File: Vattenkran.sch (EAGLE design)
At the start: 25 parts, among them J1 Power Module, J2 AVR_SPI_PRG_6OFFSET_PADS, J3 DHT11, J4 Wakeup Button, J5 RESONATOR, J6 HC-05, Q2 32KHz, U1 ATMEGA328P_PDIP, X1 VALVE

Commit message: Ape
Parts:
- removed ADC3, SCL, SDA: MCS08, solpad:MCS08
- removed C1: 10µF, adafruit:CPOL-USE2.5-6
- removed C2, C5, C6: 100nF, rcl:C-EUC0805
- removed J2: AVR_SPI_PRG_6OFFSET_PADS, SparkFun-Connectors:AVR_SPI_PRG_6OFFSET_PADS
- removed J3: DHT11, SparkFun-Connectors:M03LONGPADS
- removed J5: RESONATOR, SparkFun-Connectors:M03LONGPADS
- removed J6: HC-05, SparkFun-Connectors:M06LONGPADS
- removed R4: 22K, resistor:R-EU_R0805
- removed R5: 68K, resistor:R-EU_R0805
- removed R6: 4.7K, resistor:R-EU_R0805
- removed U1: ATMEGA328P_PDIP, SparkFun-DigitalIC:ATMEGA328P_PDIP
- removed X1: VALVE, con-wago-500:W237-102
- added U$2: BATTERY_CHARGER, breakout-modules:BATTERY_CHARGER
- added U$4: HM10_BLUETOOTH_MODULE, breakout-modules:HM10_BLUETOOTH_MODULE
- added U$5: QSKJ_BOOST_MODULE, breakout-modules:QSKJ_BOOST_MODULE
- added U$6: XL6009_BOOST_MODULE, breakout-modules:XL6009_BOOST_MODULE
- J1: value Power Module -> Battery; device SparkFun-Connectors:M08LONGPADS -> SparkFun-Connectors:M02PTH3
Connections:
- removed net !RESET: J2.5, U1.PC6(/RESET)
- removed net !VALVE_CTL: J1.5, U1.PB2(SS/OC1B)
- removed net ADC3: ADC3.MP, U1.PC3(ADC3)
- removed net BT_ENABLE: J6.1, U1.PD4(XCK/T0)
- removed net BT_VCC: J6.2, U$3.DRAIN
- removed net I_PANEL_SENSE: J1.7, U1.PC2(ADC2)
- removed net MISO: J2.1, U1.PB4(MISO)
- removed net MOSI: J2.4, U1.PB3(MOSI/OC2)
- removed net N$1: J5.3, U1.PB6(XTAL1/TOSC1)
- removed net N$18: C5.1, U1.AREF
- removed net SCK: J2.3, U1.PB5(SCK)
- removed net SCL: SCL.MP, U1.PC5(ADC5/SCL)
- removed net SDA: SDA.MP, U1.PC4(ADC4/SDA)
- removed net TEMP_SENSE: J3.3, R6.1, U1.PB1(OC1A)
- removed net VALVE_POWER: J1.4, LED1.A, X1-1.KL
- removed net VCC: C1.+, C2.1, C6.1, J1.2, J2.2, J3.2, R1.1, R6.2, U$1.VCC, U$3.SOURCE, U1.AVCC, U1.VCC
- removed net V_BATT_SENSE: R4.1, R5.2, U1.PC0(ADC0)
- removed net V_IN_UNREG_3_6: J1.3, R5.1
- removed net V_PANEL_SENSE: J1.6, U1.PC1(ADC1)
- new net BT_BRK: U$4.BRK
- new net BT_GND: U$4.GND
- new net BT_VCC33: U$4.VCC
- new net N$123: LED1.A, U$3.DRAIN, U$6.V_IN
- new net VCC33: U$1.VCC, U$5.V_OUT
- new net VCC5: U$2.V_OUT, U$5.V_IN
- new net V_BATT+: J1.2, R1.1, U$3.SOURCE
- net BT_POWER_ENABLE: no longer U1.PD5(T1)
- net BT_RX: now also U$4.RX; no longer J6.4, U1.PD0(RXD)
- net BT_STATE: now also U$4.STATE; no longer J6.6, U1.PD2(INT0)
- net BT_TX: now also U$4.TX; no longer J6.5, U1.PD1(TXD)
- net BUTTON_WAKEUP_INT: no longer U1.PD3(INT1)
- net GND: now also U$2.GND@1, U$2.GND@2, U$5.GND@1, U$5.GND@2, U$6.V_IN_GND, U$6.V_OUT_GND; no longer C1.-, C2.2, C5.2, C6.2, J2.6, J3.1, J5.2, J6.3, R4.2, U1.GND@1, U1.GND@2, X1-2.KL
- net N$2: now also U$2.V_IN; no longer J5.1, U1.PB7(XTAL2/TOSC2)
- net RTC_CE: no longer U1.PD6(AIN0)
- net RTC_IO: no longer U1.PD7(AIN1)
- net RTC_SCLK: no longer U1.PB0(ICP)
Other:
- note added: "Battery charger"
- note added: "Bluetooth"
- note added: "Logic supply"
- note added: "Valve power output"
- note removed: "BT power switch"
- note removed: "Bluetooth module Power requirement 40mA See http://www.tiny-labs.com/projects/electronics-projects/-part-hc-06-bluetooth-to-serial-adapter"
- note removed: "Pullup for DHT11 temp sensor"
- note removed: "Sensing lipo voltage (2.5-4.5 v) Using 1.1v internal bandgap reference 50µA @ 4.5V"
- note removed: "Valve output indicator"
- moved on the sheet: J4, LED1, Q2, R1, R3, SUPERCAP, U$1, U$3

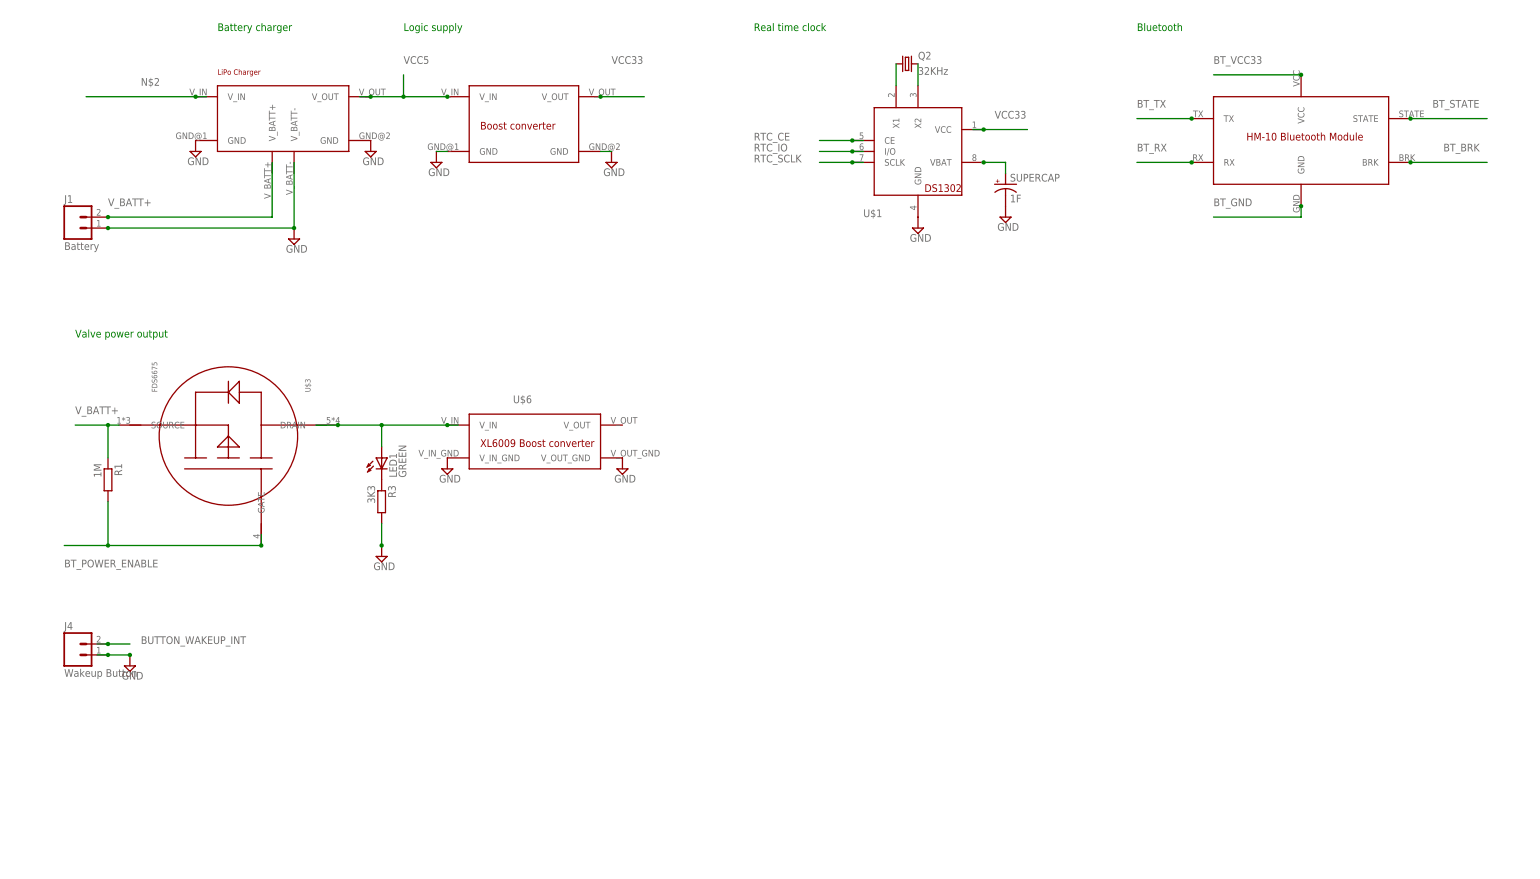
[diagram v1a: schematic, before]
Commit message: Solar input
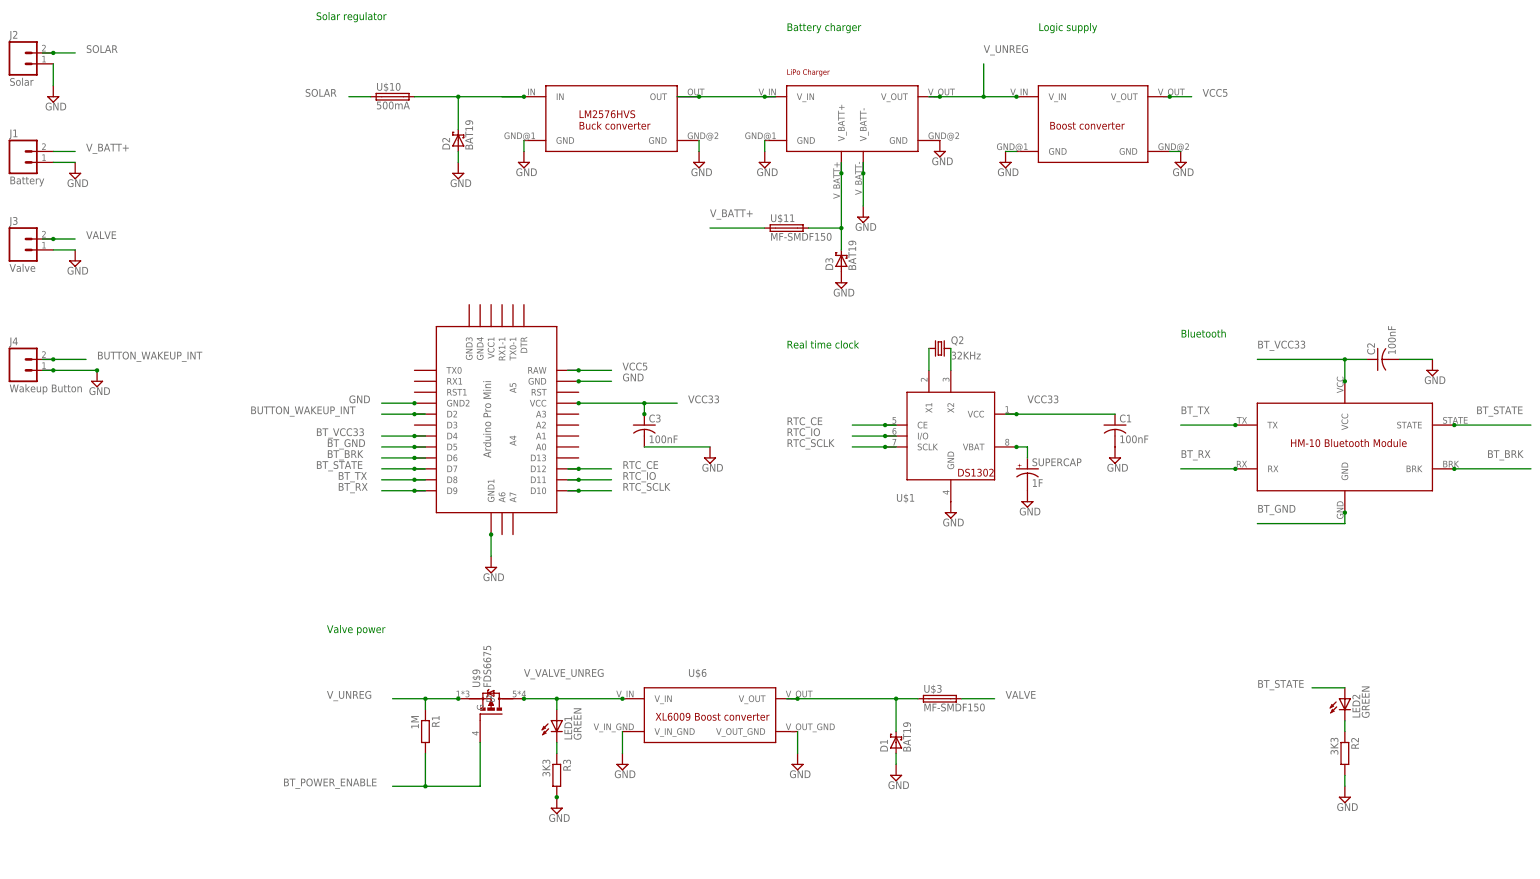
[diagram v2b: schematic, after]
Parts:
- added C1, C2, C3: 100nF, resistor:C-USC0805
- added D1, D2, D3: BAT19, diode:BAT19
- added J2: Solar, SparkFun-Connectors:M02PTH3
- added J3: Valve, SparkFun-Connectors:M02PTH3
- added LED2: GREEN, led:LED3MM
- added R2: 3K3, resistor:R-EU_R0805
- added U$10: 500mA, fuse:MF-SMDF150
- added U$11: MF-SMDF150, fuse:MF-SMDF150
- added U$7: ABK-PRO-MINI, Arduino-clone:ABK-PRO-MINI
- added U$8: LM2576HVS_BUCK_MODULE, breakout-modules:LM2576HVS_BUCK_MODULE
- added U$9: FDS6675, Semiconductors:FDS6675
- U$3: value FDS6675 -> MF-SMDF150; device FDS6675:FDS6675 -> fuse:MF-SMDF150
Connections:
- net VBATT renamed SUPERCAP
- removed net N$123: LED1.A, U$3.DRAIN, U$6.V_IN
- new net N$1: D2.C, U$10.2, U$8.IN
- new net N$3: LED2.C, R2.1
- new net N$36: D3.C, U$11.2, U$2.V_BATT+
- new net N$6: D1.C, U$3.1, U$6.V_OUT
- new net SOLAR: J2.2, U$10.1
- new net VALVE: J3.2, U$3.2
- new net V_UNREG: R1.1, U$2.V_OUT, U$5.V_IN, U$9.S
- new net V_VALVE_UNREG: LED1.A, U$6.V_IN, U$9.D
- net BT_BRK: now also U$7.D6
- net BT_GND: now also U$7.D5
- net BT_POWER_ENABLE: now also U$9.G; no longer U$3.GATE
- net BT_RX: now also U$7.D9
- net BT_STATE: now also LED2.A, U$7.D7
- net BT_TX: now also U$7.D8
- net BT_VCC33: now also C2.1, U$7.D4
- net BUTTON_WAKEUP_INT: now also U$7.D2
- net GND: now also C1.2, C2.2, C3.2, D1.A, D2.A, D3.A, J2.1, J3.1, R2.2, U$2.V_BATT-, U$7.GND, U$7.GND1, U$7.GND2, U$8.GND@1, U$8.GND@2
- net N$2: now also U$8.OUT
- net RTC_CE: now also U$7.D12
- net RTC_IO: now also U$7.D11
- net RTC_SCLK: now also U$7.D10
- net VCC33: now also C1.1, C3.1, U$7.VCC; no longer U$5.V_OUT
- net VCC5: now also U$5.V_OUT, U$7.RAW; no longer U$2.V_OUT, U$5.V_IN
- net V_BATT+: now also U$11.1; no longer R1.1, U$3.SOURCE
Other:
- note added: "Solar regulator"
- note added: "Valve power"
- note removed: "Valve power output"
- moved on the sheet: J1, J4, LED1, Q2, R1, R3, SUPERCAP, U$1, U$6

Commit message: Fixes
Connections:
- net N$4: now also Q2.2; no longer Q2.1
- net N$5: now also Q2.1; no longer Q2.2
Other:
- note added: "FIXME: High leakage current?"
- moved on the sheet: Q2
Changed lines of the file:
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@@
 <text x="-30.48" y="109.22" size="1.778" layer="91">Solar regulator</text>
 <text x="-27.94" y="-33.02" size="1.778" layer="91">Valve power</text>
+<text x="96.52" y="50.8" size="1.778" layer="91">FIXME: High leakage current?</text>
 </plain>
 <instances>
 <instance part="U$1" gate="G$1" x="116.84" y="12.7"/>
 <instance part="SUPPLY9" gate="GND" x="116.84" y="-5.08"/>
-<instance part="Q2" gate="G$1" x="114.3" y="33.02"/>
+<instance part="Q2" gate="G$1" x="114.3" y="35.56" rot="R180"/>
 <instance part="SUPERCAP" gate="G$1" x="134.62" y="5.08"/>
 <instance part="SUPPLY10" gate="GND" x="134.62" y="-2.54"/>
@@
 <net name="RTC_CE" class="0">
 <segment>
-<wire x1="104.14" y1="15.24" x2="101.6" y2="15.24" width="0.1524" layer="91"/>
 <pinref part="U$1" gate="G$1" pin="CE"/>
 <junction x="101.6" y="15.24"/>
@@
 <net name="RTC_IO" class="0">
 <segment>
-<wire x1="104.14" y1="12.7" x2="101.6" y2="12.7" width="0.1524" layer="91"/>
 <pinref part="U$1" gate="G$1" pin="I/O"/>
 <junction x="101.6" y="12.7"/>
@@
 <net name="RTC_SCLK" class="0">
 <segment>
-<wire x1="104.14" y1="10.16" x2="101.6" y2="10.16" width="0.1524" layer="91"/>
 <pinref part="U$1" gate="G$1" pin="SCLK"/>
 <junction x="101.6" y="10.16"/>
@@
 </segment>
 </net>
-<net name="N$4" class="0">
-<segment>
-<pinref part="U$1" gate="G$1" pin="X1"/>
-<pinref part="Q2" gate="G$1" pin="1"/>
-<wire x1="111.76" y1="27.94" x2="111.76" y2="33.02" width="0.1524" layer="91"/>
-</segment>
-</net>
-<net name="N$5" class="0">
-<segment>
-<pinref part="U$1" gate="G$1" pin="X2"/>
-<pinref part="Q2" gate="G$1" pin="2"/>
-<wire x1="116.84" y1="27.94" x2="116.84" y2="33.02" width="0.1524" layer="91"/>
-</segment>
-</net>
 <net name="SUPERCAP" class="0">
 <segment>
 <pinref part="U$1" gate="G$1" pin="VBAT"/>
 <pinref part="SUPERCAP" gate="G$1" pin="+"/>
-<wire x1="132.08" y1="10.16" x2="134.62" y2="10.16" width="0.1524" layer="91"/>
-<wire x1="134.62" y1="10.16" x2="134.62" y2="7.62" width="0.1524" layer="91"/>
+<wire x1="132.08" y1="10.16" x2="134.62" y2="7.62" width="0.1524" layer="91"/>
 <junction x="132.08" y="10.16"/>
 </segment>
@@
 <net name="VCC33" class="0">
 <segment>
-<wire x1="129.54" y1="17.78" x2="132.08" y2="17.78" width="0.1524" layer="91"/>
 <label x="134.62" y="20.32" size="1.778" layer="95"/>
 <pinref part="U$1" gate="G$1" pin="VCC"/>
@@
 </segment>
 </net>
+<net name="N$4" class="0">
+<segment>
+<pinref part="Q2" gate="G$1" pin="2"/>
+<pinref part="U$1" gate="G$1" pin="X1"/>
+<wire x1="111.76" y1="35.56" x2="111.76" y2="27.94" width="0.1524" layer="91"/>
+</segment>
+</net>
+<net name="N$5" class="0">
+<segment>
+<pinref part="U$1" gate="G$1" pin="X2"/>
+<pinref part="Q2" gate="G$1" pin="1"/>
+<wire x1="116.84" y1="27.94" x2="116.84" y2="35.56" width="0.1524" layer="91"/>
+</segment>
+</net>

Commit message: Layout
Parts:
- removed D1, D2, D3: BAT19, diode:BAT19
- removed J1: Battery, SparkFun-Connectors:M02PTH3
- removed J2: Solar, SparkFun-Connectors:M02PTH3
- removed J3: Valve, SparkFun-Connectors:M02PTH3
- removed J4: Wakeup Button, SparkFun-Connectors:M02PTH3
- removed LED1: GREEN, led:LED3MM
- removed R1: 1M, resistor:R-EU_R0805
- removed R3: 3K3, resistor:R-EU_R0805
- removed U$10: 500mA, fuse:MF-SMDF150
- removed U$11, U$3: MF-SMDF150, fuse:MF-SMDF150
- removed U$2: BATTERY_CHARGER, breakout-modules:BATTERY_CHARGER
- removed U$5: QSKJ_BOOST_MODULE, breakout-modules:QSKJ_BOOST_MODULE
- removed U$6: XL6009_BOOST_MODULE, breakout-modules:XL6009_BOOST_MODULE
- removed U$8: LM2576HVS_BUCK_MODULE, breakout-modules:LM2576HVS_BUCK_MODULE
- removed U$9: FDS6675, Semiconductors:FDS6675
- added TP1, TP2, TP3: TPB1,27, testpad:TPB1,27
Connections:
- removed net BT_POWER_ENABLE: R1.2, U$9.G
- removed net N$1: D2.C, U$10.2, U$8.IN
- removed net N$2: U$2.V_IN, U$8.OUT
- removed net N$36: D3.C, U$11.2, U$2.V_BATT+
- removed net N$6: D1.C, U$3.1, U$6.V_OUT
- removed net N$9: LED1.C, R3.1
- removed net SOLAR: J2.2, U$10.1
- removed net VALVE: J3.2, U$3.2
- removed net V_BATT+: J1.2, U$11.1
- removed net V_UNREG: R1.1, U$2.V_OUT, U$5.V_IN, U$9.S
- removed net V_VALVE_UNREG: LED1.A, U$6.V_IN, U$9.D
- new net VALVE_ENABLE: TP2.TP, U$7.A0
- net BUTTON_WAKEUP_INT: now also TP3.TP; no longer J4.2
- net GND: no longer D1.A, D2.A, D3.A, J1.1, J2.1, J3.1, J4.1, R3.2, U$2.GND@1, U$2.GND@2, U$2.V_BATT-, U$5.GND@1, U$5.GND@2, U$6.V_IN_GND, U$6.V_OUT_GND, U$8.GND@1, U$8.GND@2
- net VCC33: no longer C3.1
- net VCC5: now also C3.1, TP1.TP; no longer U$5.V_OUT
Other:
- note removed: "Battery charger"
- note removed: "FIXME: High leakage current?"
- note removed: "Logic supply"
- note removed: "Solar regulator"
- note removed: "Valve power"
- moved on the sheet: C2, C3, LED2, R2
